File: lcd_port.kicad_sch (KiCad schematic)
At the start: 6 parts, among them J3 TE_4-1734592-0, Q2 PMBT2222A

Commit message: mera
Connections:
- no-connect marks 0 -> 22
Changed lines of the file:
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@@
 		(color 0 0 0 0)
+	)
+	(no_connect
+		(at 92.71 101.6)
+	)
+	(no_connect
+		(at 69.85 101.6)
+	)
+	(no_connect
+		(at 140.97 101.6)
+	)
+	(no_connect
+		(at 107.95 101.6)
+	)
+	(no_connect
+		(at 148.59 101.6)
+	)
+	(no_connect
+		(at 143.51 101.6)
+	)
+	(no_connect
+		(at 146.05 101.6)
+	)
+	(no_connect
+		(at 105.41 101.6)
+	)
+	(no_connect
+		(at 102.87 101.6)
+	)
+	(no_connect
+		(at 95.25 101.6)
+	)
+	(no_connect
+		(at 87.63 101.6)
+	)
+	(no_connect
+		(at 85.09 101.6)
+	)
+	(no_connect
+		(at 82.55 101.6)
+	)
+	(no_connect
+		(at 74.93 101.6)
+	)
+	(no_connect
+		(at 120.65 101.6)
+	)
+	(no_connect
+		(at 72.39 101.6)
+	)
+	(no_connect
+		(at 100.33 101.6)
+	)
+	(no_connect
+		(at 90.17 101.6)
+	)
+	(no_connect
+		(at 97.79 101.6)
+	)
+	(no_connect
+		(at 77.47 101.6)
+	)
+	(no_connect
+		(at 80.01 101.6)
+	)
+	(no_connect
+		(at 130.81 101.6)
 	)
 	(wire

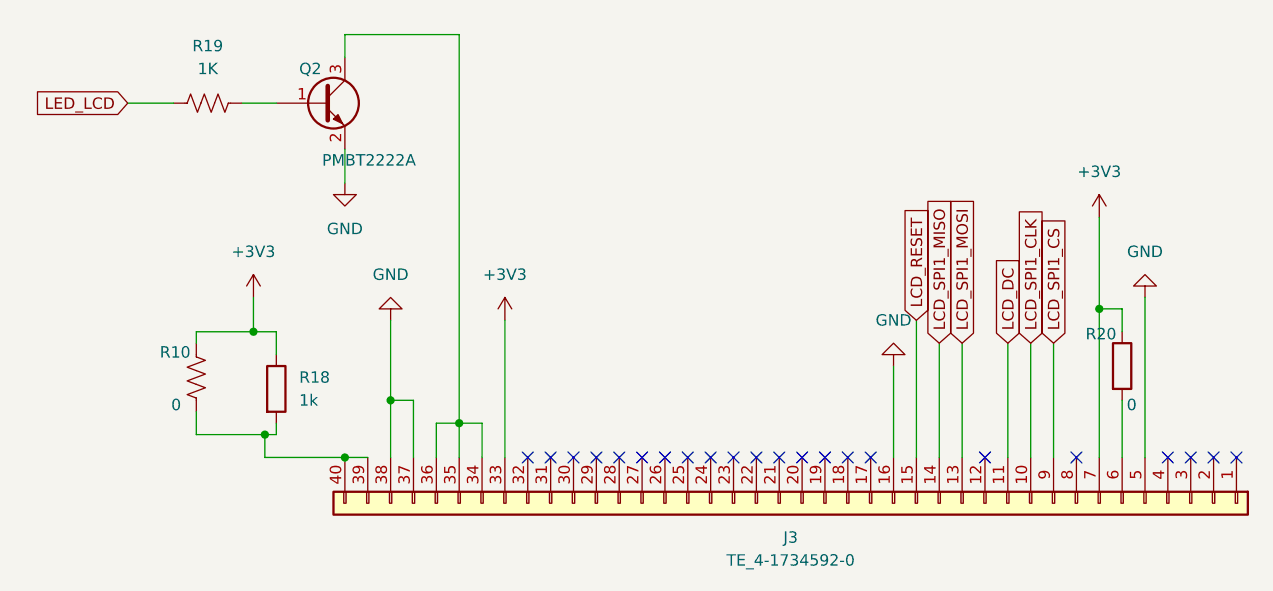
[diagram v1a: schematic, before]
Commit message: add revision to motor
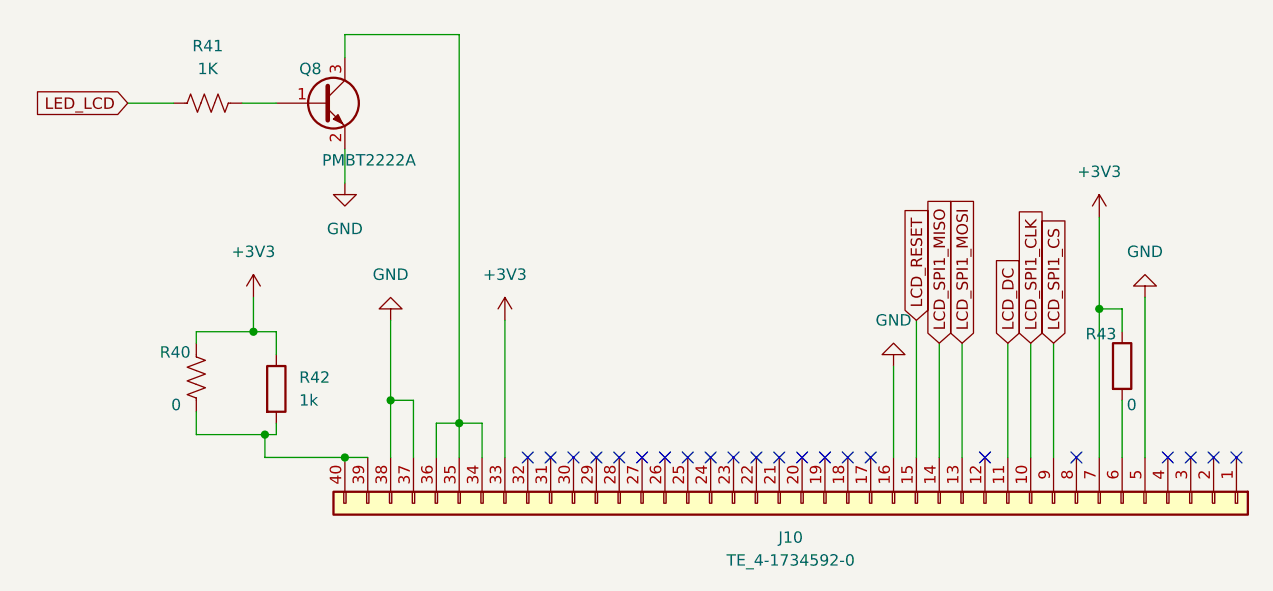
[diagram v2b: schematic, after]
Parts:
- renumbered J3 to J10, Q2 to Q8, R10 to R40, R19 to R41, R18 to R42, R20 to R43

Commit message: del some
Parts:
- renumbered J10 to J11
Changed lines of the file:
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@@
 		(dnp no)
 		(fields_autoplaced yes)
-		(property "Reference" "J10"
+		(property "Reference" "J11"
 			(at 99.06 110.49 90)
 			(effects
@@
 			(project ""
 				(path "/0db193be-516d-4409-bb62-b8733a9e8874/acf1c912-3329-4b6f-9e80-11dbc1fdd98d"
-					(reference "J10")
+					(reference "J11")
 					(unit 1)
 				)

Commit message: dad
da
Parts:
- J11: now not fitted
- Q8: Manufacturer_Part_Number (none) -> PMBT2222A,215
- R40, R43: Manufacturer_Part_Number (none) -> RC0402FR-070RL
- R41: Manufacturer_Part_Number (none) -> 0402WGF1001TCE
- R42: value 1k -> 1K; Manufacturer_Part_Number (none) -> 0402WGF1001TCE
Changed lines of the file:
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@@
 			)
 		)
-		(property "Manufacturer_Part_Number" ""
+		(property "Manufacturer_Part_Number" "RC0402FR-070RL"
 			(at 33.02 92.71 0)
 			(effects
@@
 		)
 		(property "Value2" ""
+			(at 33.02 92.71 0)
+			(effects
+				(font
+					(size 1.27 1.27)
+				)
+			)
+		)
+		(property "partNum" ""
 			(at 33.02 92.71 0)
 			(effects
@@
 			)
 		)
-		(property "Manufacturer_Part_Number" ""
+		(property "Manufacturer_Part_Number" "PMBT2222A,215"
 			(at 46.99 62.23 0)
 			(effects
@@
 		)
 		(property "Value2" ""
+			(at 46.99 62.23 0)
+			(effects
+				(font
+					(size 1.27 1.27)
+				)
+			)
+		)
+		(property "partNum" ""
 			(at 46.99 62.23 0)
 			(effects
@@
 			)
 		)
-		(property "Value" "1k"
+		(property "Value" "1K"
 			(at 44.45 95.2499 0)
 			(effects
@@
 			)
 		)
-		(property "Manufacturer_Part_Number" ""
+		(property "Manufacturer_Part_Number" "0402WGF1001TCE"
 			(at 41.91 93.98 0)
 			(effects
@@
 		)
 		(property "Value2" ""
+			(at 41.91 93.98 0)
+			(effects
+				(font
+					(size 1.27 1.27)
+				)
+			)
+		)
+		(property "partNum" ""
 			(at 41.91 93.98 0)
 			(effects
@@
 		(in_bom yes)
 		(on_board yes)
-		(dnp no)
+		(dnp yes)
 		(fields_autoplaced yes)
 		(property "Reference" "J11"
@@
 		)
 		(property "Value2" ""
+			(at 100.33 106.68 0)
+			(effects
+				(font
+					(size 1.27 1.27)
+				)
+			)
+		)
+		(property "partNum" ""
 			(at 100.33 106.68 0)
 			(effects
@@
 			)
 		)
-		(property "Manufacturer_Part_Number" ""
+		(property "Manufacturer_Part_Number" "RC0402FR-070RL"
 			(at 135.89 91.44 0)
 			(effects
@@
 		)
 		(property "Value2" ""
+			(at 135.89 91.44 0)
+			(effects
+				(font
+					(size 1.27 1.27)
+				)
+			)
+		)
+		(property "partNum" ""
 			(at 135.89 91.44 0)
 			(effects
@@
 			)
 		)
-		(property "Manufacturer_Part_Number" ""
+		(property "Manufacturer_Part_Number" "0402WGF1001TCE"
 			(at 34.29 62.23 0)
 			(effects
@@
 			(at 34.29 62.23 0)
 			(effects
+				(font
+					(size 1.27 1.27)
+				)
+			)
+		)
+		(property "partNum" ""
+			(at 34.29 62.23 0)
+			(effects

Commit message: gema
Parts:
- Q8:  LCSC Part # (none) -> C23869
- R40, R43:  LCSC Part # (none) -> C106231
- R41, R42:  LCSC Part # (none) -> C11702
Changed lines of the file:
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@@
 	(paper "A4")
+	(junction
+		(at 105.41 83.82)
+		(diameter 0)
+		(color 0 0 0 0)
+	)
 	(junction
 		(at 133.35 85.09)
@@
 	)
 	(junction
+		(at 118.11 93.98)
+		(diameter 0)
+		(color 0 0 0 0)
+	)
+	(junction
 		(at 39.37 87.63)
 		(diameter 0)
@@
 	(wire
 		(pts
+			(xy 105.41 93.98) (xy 118.11 93.98)
+		)
+		(stroke
+			(width 0)
+			(type default)
+		)
+	)
+	(wire
+		(pts
 			(xy 59.69 97.79) (xy 62.23 97.79)
 		)
@@
 	(wire
 		(pts
+			(xy 105.41 76.2) (xy 105.41 83.82)
+		)
+		(stroke
+			(width 0)
+			(type default)
+		)
+	)
+	(wire
+		(pts
 			(xy 135.89 87.63) (xy 135.89 85.09)
 		)
@@
 	(wire
 		(pts
+			(xy 105.41 83.82) (xy 105.41 93.98)
+		)
+		(stroke
+			(width 0)
+			(type default)
+		)
+	)
+	(wire
+		(pts
 			(xy 128.27 88.9) (xy 128.27 101.6)
 		)
@@
 	(wire
 		(pts
+			(xy 118.11 93.98) (xy 118.11 101.6)
+		)
+		(stroke
+			(width 0)
+			(type default)
+		)
+	)
+	(wire
+		(pts
 			(xy 39.37 87.63) (xy 41.91 87.63)
 		)
@@
 	(wire
 		(pts
-			(xy 118.11 88.9) (xy 118.11 101.6)
+			(xy 101.6 83.82) (xy 105.41 83.82)
+		)
+		(stroke
+			(width 0)
+			(type default)
+		)
+	)
+	(wire
+		(pts
+			(xy 118.11 88.9) (xy 118.11 93.98)
 		)
 		(stroke
@@
 		)
 	)
+	(global_label "LCD_SPI1_MOSI"
+		(shape input)
+		(at 105.41 76.2 180)
+		(fields_autoplaced yes)
+		(effects
+			(font
+				(size 1.27 1.27)
+			)
+			(justify right)
+		)
+		(property "Intersheetrefs" "${INTERSHEET_REFS}"
+			(at 88.0315 76.2 0)
+			(effects
+				(font
+					(size 1.27 1.27)
+				)
+				(justify right)
+				(hide yes)
+			)
+		)
+	)
 	(global_label "LCD_RESET"
 		(shape input)
@@
 		(property "Intersheetrefs" "${INTERSHEET_REFS}"
 			(at 14.432 62.23 0)
+			(effects
+				(font
+					(size 1.27 1.27)
+				)
+				(justify right)
+				(hide yes)
+			)
+		)
+	)
+	(global_label "LPSPI1_SDI"
+		(shape input)
+		(at 101.6 83.82 180)
+		(fields_autoplaced yes)
+		(effects
+			(font
+				(size 1.27 1.27)
+			)
+			(justify right)
+		)
+		(property "Intersheetrefs" "${INTERSHEET_REFS}"
+			(at 87.971 83.82 0)
 			(effects
 				(font
@@
 			)
 		)
+		(property " LCSC Part #" "C106231"
+			(at 33.02 92.71 0)
+			(effects
+				(font
+					(size 1.27 1.27)
+				)
+				(hide yes)
+			)
+		)
 		(pin "1"
 		)
@@
 					(size 1.27 1.27)
 				)
+			)
+		)
+		(property " LCSC Part #" "C23869"
+			(at 46.99 62.23 0)
+			(effects
+				(font
+					(size 1.27 1.27)
+				)
+				(hide yes)
 			)
 		)
@@
 			)
 		)
+		(property " LCSC Part #" "C11702"
+			(at 41.91 93.98 0)
+			(effects
+				(font
+					(size 1.27 1.27)
+				)
+				(hide yes)
+			)
+		)
 		(pin "1"
 		)
@@
 			)
 		)
+		(property " LCSC Part #" ""
+			(at 100.33 106.68 90)
+			(effects
+				(font
+					(size 1.27 1.27)
+				)
+				(hide yes)
+			)
+		)
 		(pin "26"
 		)
@@
 					(size 1.27 1.27)
 				)
+			)
+		)
+		(property " LCSC Part #" "C106231"
+			(at 135.89 91.44 0)
+			(effects
+				(font
+					(size 1.27 1.27)
+				)
+				(hide yes)
 			)
 		)
@@
 			)
 		)
+		(property " LCSC Part #" "C11702"
+			(at 34.29 62.23 90)
+			(effects
+				(font
+					(size 1.27 1.27)
+				)
+				(hide yes)
+			)
+		)
